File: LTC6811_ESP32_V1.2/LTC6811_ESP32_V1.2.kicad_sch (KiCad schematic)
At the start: 16 parts, among them J2 OLED /NC, J31 CAN /NC, J4 USB, Q1 BSS138

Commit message: Add files via upload
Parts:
- added J10, J11, J12, J9: Hole /NC, MountingHole:MountingHole_3.2mm_M3_ISO7380_Pad, symbol Connector_Generic:Conn_01x01
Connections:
- net CAN/5V_CAN: now also J31.4 (Pin_4); no longer J31.1 (Pin_1)
- net CAN/CAN_GND: now also J31.1 (Pin_1); no longer J31.4 (Pin_4)
- net MCU/OLED_RST: now also J2.2 (Pin_2), R6.1; no longer J2.3 (Pin_3), R7.2
- net MCU/OLED_SDA: now also J2.3 (Pin_3), R7.2; no longer J2.2 (Pin_2), R6.1
- no-connect marks 1 -> 5
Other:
- sheet PowerMonitor ports: added ISO+5V; removed BAT-
- sheet PowerSupply ports: added ISO+5V; removed none

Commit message: Add files via upload
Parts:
- removed D1: LED Red, LED_SMD:LED_0603_1608Metric, symbol Device:LED
- removed R1: 470R, Resistor_SMD:R_0603_1608Metric, symbol BMS-Master-rescue:R-Device-BMS-Master-rescue
- R2, R3, R4, R5, R6, R7, R8: symbol BMS-Master-rescue:R-Device-BMS-Master-rescue -> Device:R_Small
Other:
- sheet PowerMonitor ports: added +12V; removed none
- sheet PowerSupply ports: added +12V; removed none

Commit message: Add files via upload
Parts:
- BZ1: footprint ENNOID:BUZZER -> Buzzer_Beeper:Beeper_AI-1027-TWT-5V
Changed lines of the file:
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@@
       (effects (font (size 1.27 1.27)) (justify left) hide)
     )
-    (property "Footprint" "ENNOID:BUZZER" (at 271.78 177.8 90)
+    (property "Footprint" "Buzzer_Beeper:Beeper_AI-1027-TWT-5V" (at 271.78 177.8 90)
       (effects (font (size 1.27 1.27)) hide)
     )

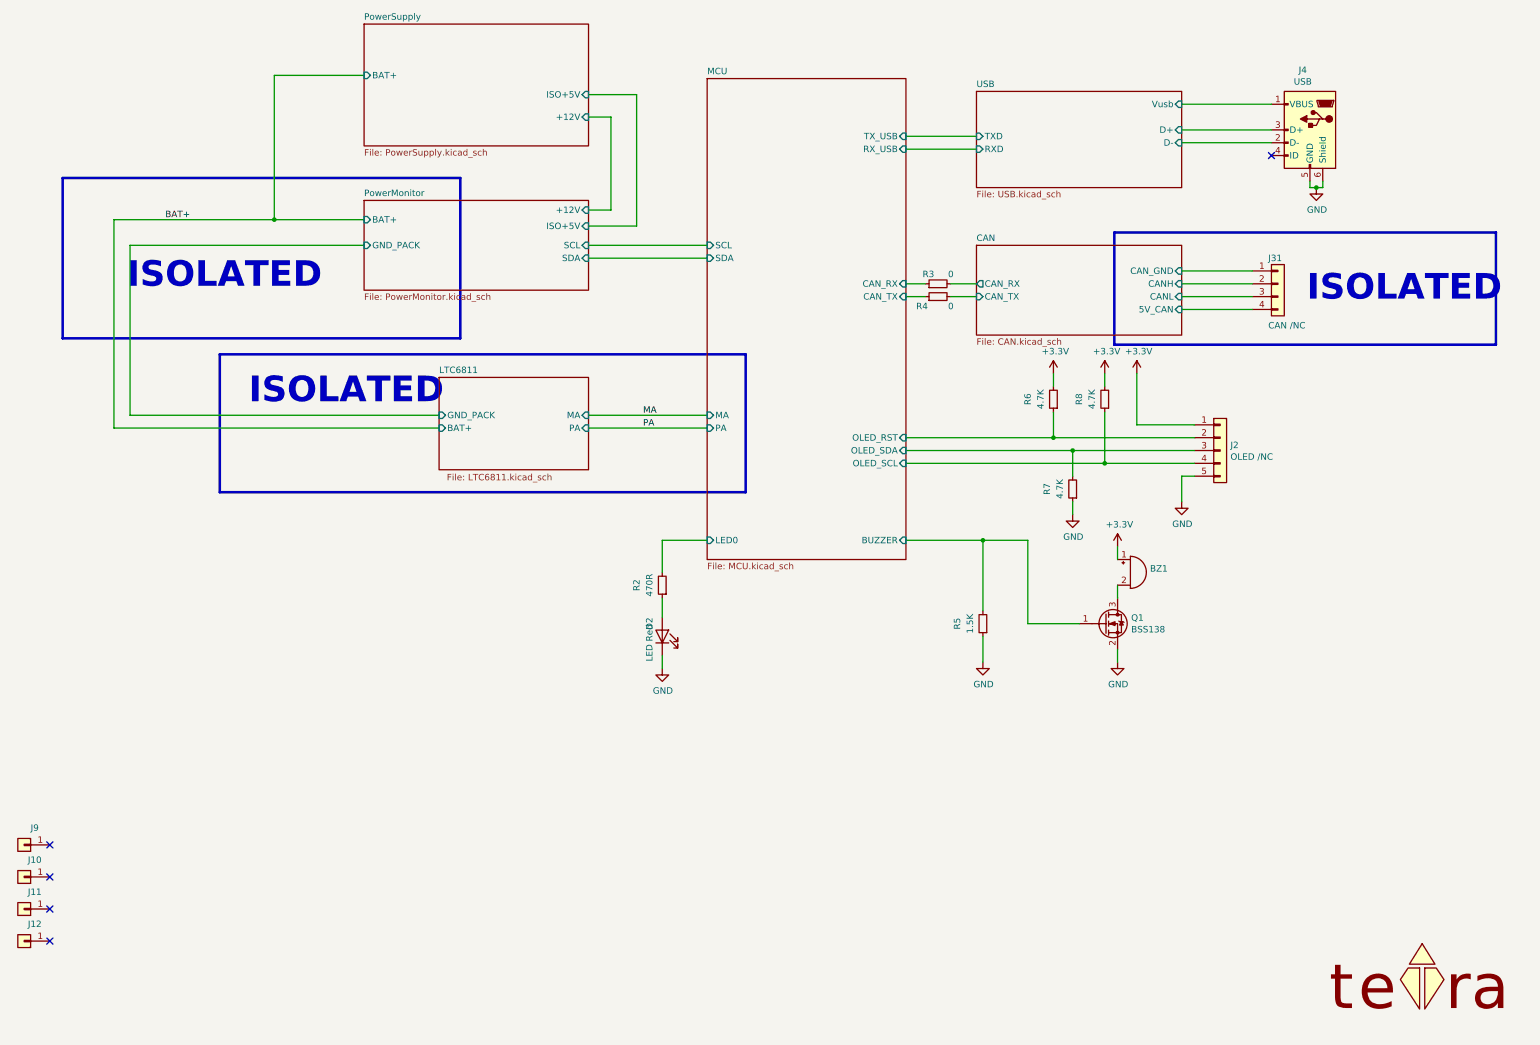
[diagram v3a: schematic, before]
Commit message: add BOM
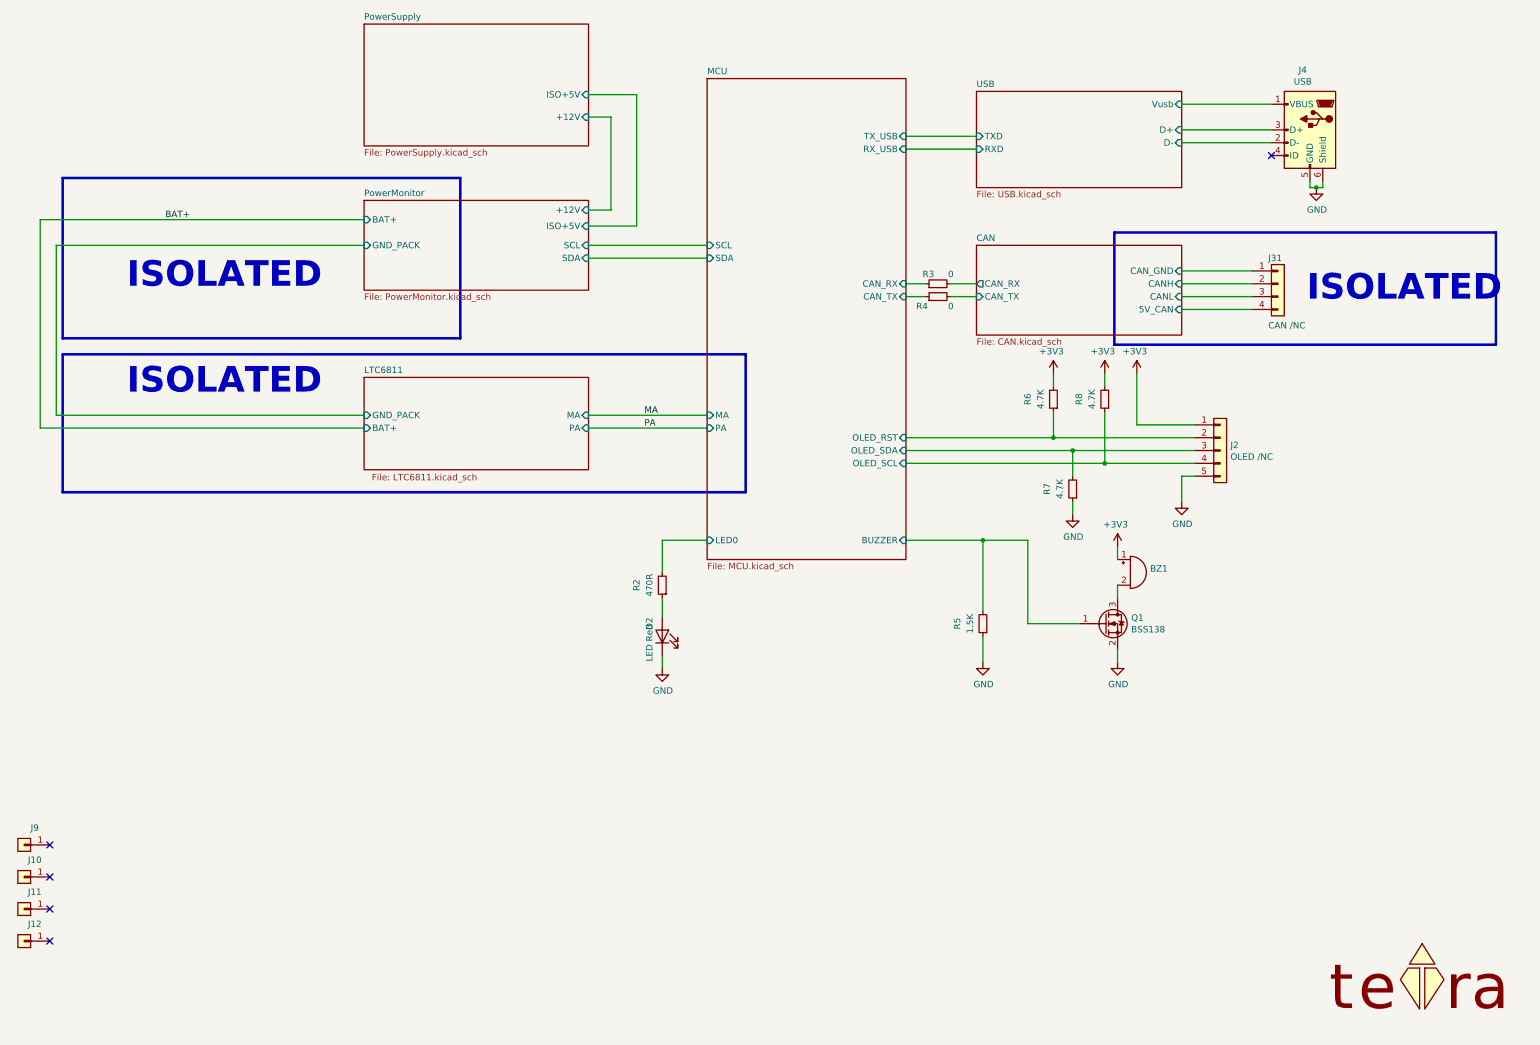
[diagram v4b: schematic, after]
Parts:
- BZ1: symbol BMS-Master-rescue:Buzzer-Device-BMS-Master-rescue -> Device:Buzzer
- J2: symbol BMS-Master-rescue:Conn_01x05-Connector_Generic-BMS-Master-rescue -> Connector_Generic:Conn_01x05; Link https://www.digikey.jp/en/products/detail/molex/0705430004/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 -> https://www.digikey.jp/en/products/detail/amphenol-cs-comme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; MPN 70543-0004 -> G800W303018EU
- J31: Link https://www.digikey.jp/en/products/detail/samtec-inc/TSW-10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 -> https://www.digikey.jp/en/products/detail/amphenol-cs-comme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; MPN TSW-104-07-G-S -> G800W304018EU
- J4: symbol BMS-Master-rescue:USB_B_Micro-Connector_Specialized-BMS-Master-rescue -> Connector:USB_B_Micro
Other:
- sheet PowerSupply ports: added none; removed BAT+
